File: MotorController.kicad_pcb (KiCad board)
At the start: 2 copper layers, 131 parts, among them IC1 ft234xd, IC2 A3921KLPTR-T, IC3 A3921KLPTR-T, J1 SH, J10 XT30, J11 XT30, J2 USB_B_Micro, J3 XA, J4 XA, J5 3020-10-0300-00, J6 SH, J7 SH, J8 3020-10-0300-00, J9 XA, Q1 GSFQ6806, Q2 GSFQ6806, Q3 GSFQ6806, Q4 SFS9Z34, Q5 GSFQ6806, Q6 SFS9Z34, SW2 BLACK, SW3 BLACK, SW4 2MS1-T1-B4-VS2-Q-E-S, SW5 RED, U1 LXES11D, U2 STM32F303K8Tx, U3 TJA1441AT, U4 TPSM13604HNDWR, U5 LMZ12002EXT, Y1 32M

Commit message: 電源回路設置完了！USB の回路設置中
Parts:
- C14, C4, IC1, R35: moved to B.Cu
- J10: value XT30 -> PA; footprint LibraryLoader:XT30PWM -> LibraryLoader:PA_01x02
- J5, J8: footprint Connector_IDC:IDC-Header_2x10_P2.54mm_Vertical -> Connector_IDC:IDC-Header_2x05_P2.54mm_Vertical
- Q1, Q2, Q3, Q5: footprint Package_SO:HSOP-8-1EP_3.9x4.9mm_P1.27mm_EP2.3x2.3mm -> Package_SO:SO-8_3.9x4.9mm_P1.27mm
- moved J2 546.5 mm to (0.00, -11.0), turned to 180 degrees
- moved J1 532.2 mm to (10.0, -11.0), turned to 0 degrees
- moved R28 336.4 mm to (475.0, 169.5), turned to 180 degrees
- moved R30 304.4 mm to (451.0, 8.00)
- moved U1 293.9 mm to (0.00, -6.00), turned to 180 degrees
- moved L1 286.8 mm to (3.00, -2.00), turned to 90 degrees
- moved D2 286.6 mm to (3.00, -6.00), turned to 90 degrees
- moved IC1 280.6 mm to (0.00, -2.00), turned to 180 degrees
- moved C3 277.6 mm to (-4.00, 0.00), turned to -90 degrees
- moved C4 277.0 mm to (3.00, -1.00), turned to -90 degrees
- moved C5 276.9 mm to (4.00, 1.00)
- moved C14 274.8 mm to (4.50, -2.00), turned to -90 degrees
- moved D13 255.5 mm to (12.0, 240.0), turned to 90 degrees
- moved C37 254.9 mm to (8.50, 215.5), turned to 90 degrees
- moved D12 254.8 mm to (15.0, 240.0), turned to 90 degrees
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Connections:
- U4 pad 8: (no net) -> GND
- U5 pad 8: (no net) -> GND
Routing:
- net Net-(Q6-G): track 0.00 -> 30.1 mm, vias 0 -> 1
- net Net-(U4-EN): track 0.00 -> 8.85 mm
- net Net-(U5-EN): track 0.00 -> 7.50 mm
- net Net-(U4-FB): track 0.00 -> 6.12 mm
- net Net-(IC1-3V3OUT): track 0.00 -> 3.54 mm
- net Net-(U4-RON): track 0.00 -> 2.90 mm
- net Net-(U5-RON): track 0.00 -> 2.90 mm
- net Net-(U4-SS): track 0.00 -> 2.66 mm
- net +5V: track 0.00 -> 1.55 mm
- added copper zone on F.Cu, net +3V3
- added copper zone on F.Cu, net +5V
- added copper zone on F.Cu, net Net-(D11-A)
- added copper zone on F.Cu, net Net-(D14-K)

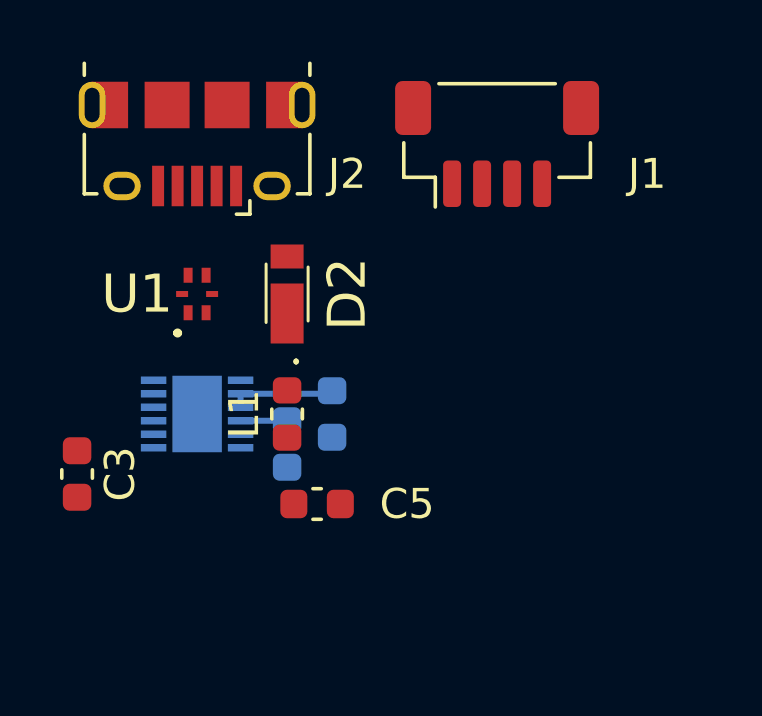
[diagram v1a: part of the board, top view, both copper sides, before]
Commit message: USB 周りの配線を少し進めた
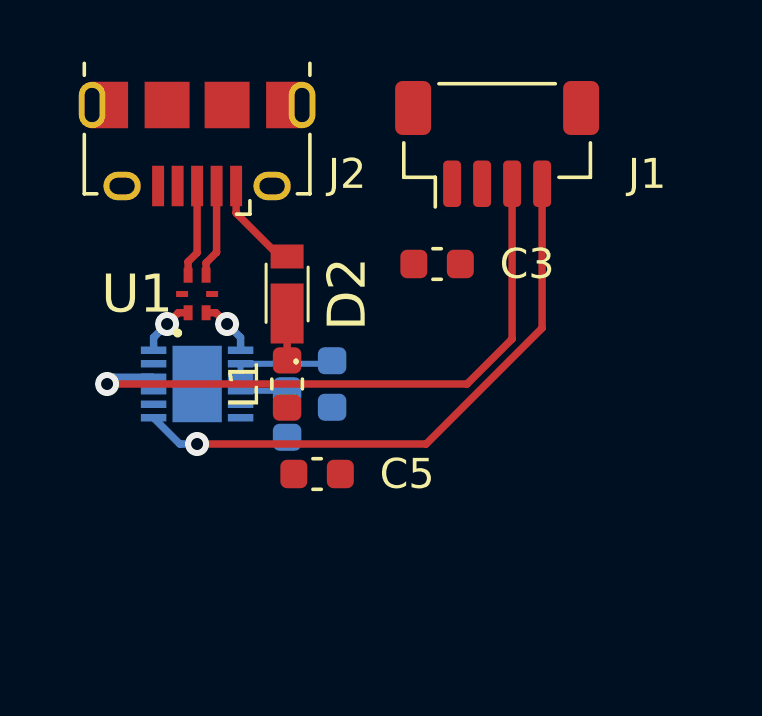
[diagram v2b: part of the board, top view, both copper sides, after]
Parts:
- moved C3 13.9 mm to (8.00, -7.00), turned to 0 degrees
- moved C14 1.00 mm to (4.50, -3.00)
- moved C4 1.00 mm to (3.00, -2.00)
- moved C5 1.00 mm to (4.00, 0.00)
- moved IC1 1.00 mm to (0.00, -3.00)
- moved L1 1.00 mm to (3.00, -3.00)
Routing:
- net Net-(IC1-RXD): track 0.00 -> 20.9 mm, vias 0 -> 1
- net Net-(IC1-TXD): track 0.00 -> 19.7 mm, vias 0 -> 1
- net Net-(D2-A): track 0.00 -> 3.20 mm
- net Net-(J2-D-): track 0.00 -> 3.12 mm
- net Net-(J2-D+): track 0.00 -> 3.10 mm
- net Net-(IC1-USBDP): track 0.00 -> 1.92 mm, vias 0 -> 1
- net Net-(IC1-USBDM): track 0.00 -> 1.92 mm, vias 0 -> 1
- net Net-(D2-K): track 0.00 -> 1.56 mm
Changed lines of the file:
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@@
   )
   (footprint "Capacitor_SMD:C_0603_1608Metric" (layer "F.Cu")
-    (at 4 1)
+    (at 4 0)
     (descr "Capacitor SMD 0603 (1608 Metric), square (rectangular) end terminal, IPC_7351 nominal, (Body size source: IPC-SM-782 page 76, https://www.pcb-3d.com/wordpress/wp-content/uploads/ipc-sm-782a_amendment_1_and_2.pdf), generated with kicad-footprint-generator")
     (tags "capacitor")
@@
   )
   (footprint "Inductor_SMD:L_0603_1608Metric" (layer "F.Cu")
-    (at 3 -2 90)
+    (at 3 -3 90)
     (descr "Inductor SMD 0603 (1608 Metric), square (rectangular) end terminal, IPC_7351 nominal, (Body size source: http://www.tortai-tech.com/upload/download/2011102023233369053.pdf), generated with kicad-footprint-generator")
     (tags "inductor")
@@
   )
   (footprint "Capacitor_SMD:C_0603_1608Metric" (layer "F.Cu")
-    (at -4 0 -90)
+    (at 8 -7)
     (descr "Capacitor SMD 0603 (1608 Metric), square (rectangular) end terminal, IPC_7351 nominal, (Body size source: IPC-SM-782 page 76, https://www.pcb-3d.com/wordpress/wp-content/uploads/ipc-sm-782a_amendment_1_and_2.pdf), generated with kicad-footprint-generator")
     (tags "capacitor")
@@
     (property "ki_keywords" "cap capacitor")
     (attr smd)
-    (fp_text reference "C3" (at 0 -1.43 90) (layer "F.SilkS")
+    (fp_text reference "C3" (at 3 0) (layer "F.SilkS")
         (effects (font (size 1 1) (thickness 0.15)))
     )
-    (fp_text value "C" (at 0 1.43 90) (layer "F.Fab")
+    (fp_text value "C" (at 0 1.43) (layer "F.Fab")
         (effects (font (size 1 1) (thickness 0.15)))
     )
-    (fp_text user "${REFERENCE}" (at 0 0 90) (layer "F.Fab")
+    (fp_text user "${REFERENCE}" (at 0 0) (layer "F.Fab")
         (effects (font (size 0.4 0.4) (thickness 0.06)))
     )
@@
     (fp_line (start 0.8 0.4) (end -0.8 0.4)
       (stroke (width 0.1) (type solid)) (layer "F.Fab"))
-    (pad "1" smd roundrect (at -0.775 0 270) (size 0.9 0.95) (layers "F.Cu" "F.Paste" "F.Mask") (roundrect_rratio 0.25)
+    (pad "1" smd roundrect (at -0.775 0) (size 0.9 0.95) (layers "F.Cu" "F.Paste" "F.Mask") (roundrect_rratio 0.25)
       (net 5 "+5V") (pintype "passive"))
-    (pad "2" smd roundrect (at 0.775 0 270) (size 0.9 0.95) (layers "F.Cu" "F.Paste" "F.Mask") (roundrect_rratio 0.25)
+    (pad "2" smd roundrect (at 0.775 0) (size 0.9 0.95) (layers "F.Cu" "F.Paste" "F.Mask") (roundrect_rratio 0.25)
       (net 2 "GND") (pintype "passive"))
     (model "${KICAD6_3DMODEL_DIR}/Capacitor_SMD.3dshapes/C_0603_1608Metric.wrl"
@@
   )
   (footprint "LibraryLoader:SON45P300X300X80-13N-D" (layer "B.Cu")
-    (at 0 -2 180)
+    (at 0 -3 180)
     (descr "ft234xd")
     (tags "Integrated Circuit")
@@
   )
   (footprint "Capacitor_SMD:C_0603_1608Metric" (layer "B.Cu")
-    (at 3 -1 -90)
+    (at 3 -2 -90)
     (descr "Capacitor SMD 0603 (1608 Metric), square (rectangular) end terminal, IPC_7351 nominal, (Body size source: IPC-SM-782 page 76, https://www.pcb-3d.com/wordpress/wp-content/uploads/ipc-sm-782a_amendment_1_and_2.pdf), generated with kicad-footprint-generator")
     (tags "capacitor")
@@
   )
   (footprint "Capacitor_SMD:C_0603_1608Metric" (layer "B.Cu")
-    (at 4.5 -2 -90)
+    (at 4.5 -3 -90)
     (descr "Capacitor SMD 0603 (1608 Metric), square (rectangular) end terminal, IPC_7351 nominal, (Body size source: IPC-SM-782 page 76, https://www.pcb-3d.com/wordpress/wp-content/uploads/ipc-sm-782a_amendment_1_and_2.pdf), generated with kicad-footprint-generator")
     (tags "capacitor")
@@
   (gr_rect (start 0 200) (end 60 250)
     (stroke (width 0.15) (type default)) (fill none) (layer "User.1"))
-  (segment (start 3 -1.775) (end 1.45 -1.775) (width 0.2) (layer "B.Cu") (net 5))
-  (segment (start 4.4 -2.675) (end 4.5 -2.775) (width 0.2) (layer "B.Cu") (net 12))
-  (segment (start 1.45 -2.675) (end 4.4 -2.675) (width 0.2) (layer "B.Cu") (net 12))
-  (segment (start 1.45 -2.225) (end 1.45 -2.675) (width 0.2) (layer "B.Cu") (net 12))
+  (segment (start 3 -2.775) (end 1.45 -2.775) (width 0.2) (layer "B.Cu") (net 5))
+  (segment (start 4.4 -3.675) (end 4.5 -3.775) (width 0.2) (layer "B.Cu") (net 12))
+  (segment (start 1.45 -3.675) (end 4.4 -3.675) (width 0.2) (layer "B.Cu") (net 12))
+  (segment (start 1.45 -3.225) (end 1.45 -3.675) (width 0.2) (layer "B.Cu") (net 12))
   (segment (start 17.54 220.365) (end 19 221.825) (width 0.15) (layer "F.Cu") (net 28))
   (segment (start 19 221.825) (end 19 223.175) (width 0.15) (layer "F.Cu") (net 28))
@@
   (segment (start 16.27 217.66) (end 16.27 219.995) (width 0.15) (layer "F.Cu") (net 32))
   (segment (start 16.27 219.995) (end 16.5 220.225) (width 0.15) (layer "F.Cu") (net 32))
+  (segment (start 3 -5.35) (end 3 -3.7875) (width 0.25) (layer "F.Cu") (net 34))
+  (segment (start 1.3 -8.7) (end 2.75 -7.25) (width 0.25) (layer "F.Cu") (net 35))
+  (segment (start 1.3 -9.6) (end 1.3 -8.7) (width 0.25) (layer "F.Cu") (net 35))
+  (segment (start 2.75 -7.25) (end 3 -7.25) (width 0.25) (layer "F.Cu") (net 35))
+  (segment (start 0.625 -5.375) (end 1 -5) (width 0.25) (layer "F.Cu") (net 39))
+  (segment (start 0.3 -5.375) (end 0.625 -5.375) (width 0.25) (layer "F.Cu") (net 39))
+  (via (at 1 -5) (size 0.8) (drill 0.4) (layers "F.Cu" "B.Cu") (net 39))
+  (segment (start 1.45 -4.55) (end 1 -5) (width 0.25) (layer "B.Cu") (net 39))
+  (segment (start 1.45 -4.125) (end 1.45 -4.55) (width 0.25) (layer "B.Cu") (net 39))
+  (segment (start 7.636396 -1) (end 0 -1) (width 0.25) (layer "F.Cu") (net 41))
+  (segment (start 11.5 -9.675) (end 11.5 -4.863604) (width 0.25) (layer "F.Cu") (net 41))
+  (segment (start 11.5 -4.863604) (end 7.636396 -1) (width 0.25) (layer "F.Cu") (net 41))
+  (via (at 0 -1) (size 0.8) (drill 0.4) (layers "F.Cu" "B.Cu") (net 41))
+  (segment (start -0.575 -1) (end -1.45 -1.875) (width 0.25) (layer "B.Cu") (net 41))
+  (segment (start 0 -1) (end -0.575 -1) (width 0.25) (layer "B.Cu") (net 41))
+  (segment (start 9 -3) (end -3 -3) (width 0.25) (layer "F.Cu") (net 43))
+  (segment (start 10.5 -4.5) (end 9 -3) (width 0.25) (layer "F.Cu") (net 43))
+  (segment (start 10.5 -9.675) (end 10.5 -4.5) (width 0.25) (layer "F.Cu") (net 43))
+  (via (at -3 -3) (size 0.8) (drill 0.4) (layers "F.Cu" "B.Cu") (net 43))
+  (segment (start -3 -3) (end -2.775 -3.225) (width 0.25) (layer "B.Cu") (net 43))
+  (segment (start -2.775 -3.225) (end -1.45 -3.225) (width 0.25) (layer "B.Cu") (net 43))
+  (segment (start -0.3 -5.375) (end -0.625 -5.375) (width 0.25) (layer "F.Cu") (net 44))
+  (segment (start -0.625 -5.375) (end -1 -5) (width 0.25) (layer "F.Cu") (net 44))
+  (via (at -1 -5) (size 0.8) (drill 0.4) (layers "F.Cu" "B.Cu") (net 44))
+  (segment (start -1.45 -4.125) (end -1.45 -4.55) (width 0.25) (layer "B.Cu") (net 44))
+  (segment (start -1.45 -4.55) (end -1 -5) (width 0.25) (layer "B.Cu") (net 44))
+  (segment (start 0.3 -7.038604) (end 0.3 -6.625) (width 0.25) (layer "F.Cu") (net 74))
+  (segment (start 0.65 -7.388604) (end 0.3 -7.038604) (width 0.25) (layer "F.Cu") (net 74))
+  (segment (start 0.65 -9.6) (end 0.65 -7.388604) (width 0.25) (layer "F.Cu") (net 74))
+  (segment (start 0 -7.375) (end -0.3 -7.075) (width 0.25) (layer "F.Cu") (net 75))
+  (segment (start -0.3 -7.075) (end -0.3 -6.625) (width 0.25) (layer "F.Cu") (net 75))
+  (segment (start 0 -9.6) (end 0 -7.375) (width 0.25) (layer "F.Cu") (net 75))
   (segment (start 492.54 234.54) (end 492 234) (width 0.15) (layer "F.Cu") (net 110))
   (segment (start 505 234.54) (end 492.54 234.54) (width 0.15) (layer "F.Cu") (net 110))

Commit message: Z 実装
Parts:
- R1, R11, R12, R13, R19, R23, R27, R28, R29, R30, R6: moved to B.Cu
- moved C31 480.9 mm to (93.5, 87.5), turned to 90 degrees
- moved C27 473.7 mm to (102.0, 82.5)
- moved C26 473.2 mm to (93.5, 84.5), turned to 90 degrees
- moved C28 469.7 mm to (107.0, 89.0)
- moved C29 468.6 mm to (107.0, 86.5), turned to -90 degrees
- moved C34 467.0 mm to (107.0, 91.5), turned to 90 degrees
- moved C2 461.6 mm to (93.5, 34.5), turned to 90 degrees
- moved C9 459.9 mm to (93.5, 37.5), turned to 90 degrees
- moved J4 458.1 mm to (70.5, 26.2), turned to -90 degrees
- moved C18 451.8 mm to (107.0, 41.5), turned to 90 degrees
- moved C6 451.7 mm to (102.0, 32.5)
- moved C7 447.2 mm to (107.0, 39.0)
- moved C8 446.6 mm to (107.0, 36.5), turned to -90 degrees
- moved D6 425.6 mm to (116.0, 45.5), turned to 90 degrees
- moved D3 425.5 mm to (116.0, 31.5), turned to 90 degrees
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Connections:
- D14 pad 2: GND -> Net-(D14-A)
- D15 pad 1: Net-(D14-K) -> Net-(D15-K)
- D15 pad 2: GND -> Net-(D15-A)
- J10 pad 1: Net-(J10-Pin_1) -> Net-(D14-A)
- J11 pad 1: Net-(J11-Pin_1) -> Net-(D15-K)
- Q4 pad 1: Net-(J10-Pin_1) -> Net-(D14-A)
- Q6 pad 1: Net-(Q6-G) -> Net-(D15-A)
- Q6 pad 3: Net-(J11-Pin_1) -> Net-(D15-K)
- R28 pad 2: Net-(J10-Pin_1) -> Net-(D14-A)
- R35 pad 1: Net-(J11-Pin_1) -> Net-(D15-K)
- R35 pad 2: Net-(Q6-G) -> Net-(D15-A)
- SW4 pad 3: Net-(Q6-G) -> Net-(D15-A)
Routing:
- net Net-(Q6-G): track 30.1 -> 0.00 mm, vias 1 -> 0
- net +5V: track 1.55 -> 22.9 mm, vias 0 -> 2
- net Net-(J4-Pin_3): track 0.00 -> 15.0 mm
- net Net-(J4-Pin_2): track 0.00 -> 15.0 mm
- net Net-(U2-PF1): track 0.00 -> 13.8 mm
- net Net-(U2-PF0): track 0.00 -> 13.7 mm
- net Net-(IC3-V5): track 0.00 -> 9.75 mm
- net Net-(IC1-CTS#): track 0.00 -> 9.21 mm
- net +3V3: track 0.00 -> 8.59 mm
- net Net-(IC3-VDSTH): track 0.00 -> 5.97 mm
- net Net-(IC3-FF1): track 0.00 -> 5.77 mm
- net Net-(IC3-FF2): track 0.00 -> 5.42 mm
- net Net-(D8-K): track 0.00 -> 5.07 mm
- net Net-(IC3-CA): track 0.00 -> 4.97 mm
- net Net-(D10-K): track 0.00 -> 4.66 mm
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- added copper zone on F.Cu, net Net-(D10-K)
- added copper zone on F.Cu, net Net-(D3-K)
- added copper zone on F.Cu, net Net-(D6-K)
- added copper zone on F.Cu, net Net-(D8-K)
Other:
- board text added: "CAN"
- board text added: "CPU"
- board text added: "DC/DC"
- board text added: "MotorDriver"
- board text added: "UART"

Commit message: CPU CAN MD DCDC の位置感決めた あとは UI
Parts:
- C20, R17, R18, R24, R25: moved to B.Cu
- moved J8 139.8 mm to (29.5, 38.0), turned to 90 degrees
- moved C11 129.6 mm to (28.0, 22.5)
- moved C12 129.6 mm to (41.0, 30.5)
- moved C13 129.6 mm to (26.0, 27.0)
- moved C15 129.6 mm to (17.5, 23.5)
- moved C17 129.6 mm to (17.5, 26.5)
- moved R9 129.6 mm to (32.5, 18.0)
- moved U2 129.6 mm to (34.5, 26.5)
- moved Y1 129.6 mm to (21.5, 27.4)
- moved R24 125.4 mm to (25.5, 34.0)
- moved D15 120.3 mm to (137.0, 100.0), turned to 180 degrees
- moved R25 119.5 mm to (31.0, 34.0)
- moved D4 115.8 mm to (24.0, 86.0), turned to 0 degrees
- moved D1 109.1 mm to (38.0, 86.0), turned to 0 degrees
- moved J5 106.7 mm to (51.0, 38.0), turned to 90 degrees
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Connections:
- IC2 pad 22: DRV1_PWML -> DRV1_PWMH
- IC2 pad 23: DRV1_PWMH -> DRV1_PWML
- U2 pad 11: Encoder_RA -> Encoder_RB
- U2 pad 18: Encoder_LB -> Encoder_LA
- U2 pad 19: Encoder_LA -> Encoder_LB
- U2 pad 7: Encoder_RB -> Encoder_RA
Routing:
- net +5V: track 22.9 -> 90.0 mm, vias 2 -> 4
- net Encoder_LB: track 0.00 -> 20.1 mm, vias 0 -> 1
- net Encoder_LA: track 0.00 -> 15.7 mm, vias 0 -> 1
- net Net-(IC1-3V3OUT): track 2.05 -> 15.3 mm, vias 0 -> 2
- net Encoder_RA: track 0.00 -> 11.9 mm, vias 0 -> 1
- net Net-(J4-Pin_3): track 15.0 -> 4.64 mm
- net Net-(J4-Pin_2): track 15.0 -> 4.64 mm
- net Net-(U2-PA12): track 0.00 -> 8.85 mm
- net Net-(U2-PA11): track 0.00 -> 7.68 mm
- net Net-(D5-A): track 0.00 -> 7.05 mm, vias 0 -> 1
- net Encoder_RB: track 0.00 -> 6.76 mm, vias 0 -> 1
- net Net-(D12-A): track 0.00 -> 1.39 mm
- net Net-(IC1-TXD): track 20.4 -> 19.2 mm
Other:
- board outline added: 95 x 102.5 mm
- board text removed: "CAN"
- board text removed: "CPU"
- board text removed: "DC/DC"
- board text removed: "MotorDriver"
- board text removed: "UART"

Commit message: GND ベタを塗る直前までやった
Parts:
- added H1: MountingHole, MountingHole:MountingHole_3.2mm_M3, F.Cu at (88.5, 28.5)
- added H2: MountingHole, MountingHole:MountingHole_3.2mm_M3, F.Cu at (39.0, 96.0)
- C23, C33, D15: moved to B.Cu
- moved R8 151.6 mm to (36.5, 18.0), turned to -90 degrees
- moved R14 150.3 mm to (34.5, 18.0), turned to -90 degrees
- moved R2 149.6 mm to (25.0, 32.0)
- moved C23 147.6 mm to (21.5, 35.0), turned to 90 degrees
- moved C21 136.4 mm to (21.0, 101.5), turned to 180 degrees
- moved SW3 128.2 mm to (21.0, 108.0), turned to -90 degrees
- moved C16 127.1 mm to (30.0, 101.5), turned to 180 degrees
- moved C33 126.5 mm to (43.0, 35.0), turned to 90 degrees
- moved SW2 119.0 mm to (30.0, 108.0), turned to -90 degrees
- moved D5 118.7 mm to (38.5, 110.0), turned to 90 degrees
- moved R10 118.6 mm to (38.5, 104.5), turned to -90 degrees
- moved C32 111.8 mm to (64.5, 21.5), turned to -90 degrees
- moved C10 111.3 mm to (46.5, 101.5), turned to 180 degrees
- moved C30 105.7 mm to (64.5, 32.5), turned to -90 degrees
- moved J7 104.7 mm to (69.5, 23.0), turned to -90 degrees
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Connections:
- D14 pad 2: Net-(D14-A) -> GND
- D15 pad 2: Net-(D15-A) -> GND
- J10 pad 1: Net-(D14-A) -> Net-(J10-Pin_1)
- Q4 pad 1: Net-(D14-A) -> Net-(J10-Pin_1)
- Q6 pad 1: Net-(D15-A) -> Net-(Q6-G)
- R28 pad 2: Net-(D14-A) -> Net-(J10-Pin_1)
- R35 pad 2: Net-(D15-A) -> Net-(Q6-G)
- SW4 pad 3: Net-(D15-A) -> Net-(Q6-G)
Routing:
- net +3V3: track 8.59 -> 294.2 mm, vias 0 -> 9
- net NRST: track 0.00 -> 147.5 mm, vias 0 -> 3
- net +5V: track 90.0 -> 214.0 mm, vias 4 -> 7
- net Net-(U2-PB5): track 0.00 -> 108.1 mm, vias 0 -> 2
- net Net-(U2-PB6): track 0.00 -> 105.8 mm, vias 0 -> 2
- net +BATT: track 0.00 -> 81.9 mm, vias 0 -> 4
- net DRV2_PHASE: track 0.00 -> 60.9 mm, vias 0 -> 2
- net Net-(J6-Pin_3): track 0.00 -> 58.1 mm, vias 0 -> 2
- net DRVx_SR: track 0.00 -> 51.7 mm, vias 0 -> 2
- net Net-(J6-Pin_2): track 0.00 -> 48.6 mm, vias 0 -> 2
- net Net-(J7-Pin_6): track 0.00 -> 41.3 mm
- net Net-(J7-Pin_4): track 0.00 -> 36.4 mm
- net Net-(J7-Pin_2): track 0.00 -> 36.2 mm
- net DRV2_PWML: track 0.00 -> 29.7 mm, vias 0 -> 2
- net DRV2_PWMH: track 0.00 -> 29.2 mm, vias 0 -> 2
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- added copper zone on F.Cu, net +BATT
- added copper zone on B.Cu, net Net-(D14-K)
- added copper zone on B.Cu, net Net-(D15-K)
- added copper zone on F.Cu, net Net-(D15-K)
- added copper zone on B.Cu, net Net-(Q6-G)
- added copper zone on F.Cu, net Net-(Q6-G)
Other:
- board text added: "RESET"
